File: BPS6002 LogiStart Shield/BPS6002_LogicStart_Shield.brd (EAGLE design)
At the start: 118.4 x 58.7 mm, 91 parts, among them J1 AUDIO-CONNECTOR-6P-SMD-344003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, Q1 MMBTA56, Q2 MMBTA56, Q3 MMBTA56, Q4 MMBTA56, Q5 MMBTA56

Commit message: LogicStart Shield V1.01
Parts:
- added AREF: (no value), adafruit:1X01
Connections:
- new net N$9: AREF.1, H1.AREF
- net 3V3: now also JP2.1, JP2.2, JP2.3, JP2.4, JP2.5, JP2.6
- net 5V0: no longer H1.AREF, JP2.1, JP2.2, JP2.3, JP2.4, JP2.5, JP2.6
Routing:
- net 5V0: track 135.6 -> 40.7 mm, vias 3 -> 2
- net 3V3: track 21.1 -> 31.3 mm
- net N$9: track 0.00 -> 5.21 mm
- net DIR_LEFT: track 39.7 -> 43.3 mm
- net DIR_DOWN: track 53.7 -> 56.5 mm
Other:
- board text added: "Get Started at LogicShield.GadgetFactory.Net"
- board text added: "LogicStart Shield V1.01"
- board text removed: "5V"
- board text removed: "Get Started at learn.GadgetFactory.net/LogicStart"
- board text removed: "LogicStart Shield V1.0"
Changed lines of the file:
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@@
 <layer number="220" name="220bmp" color="21" fill="1" visible="no" active="no"/>
 <layer number="221" name="221bmp" color="22" fill="1" visible="no" active="no"/>
+<layer number="222" name="222bmp" color="23" fill="1" visible="no" active="no"/>
 <layer number="223" name="223bmp" color="24" fill="1" visible="no" active="no"/>
 <layer number="224" name="224bmp" color="25" fill="1" visible="no" active="no"/>
@@
 <wire x1="1.016" y1="0" x2="1.016" y2="55.88" width="0.254" layer="20"/>
 <text x="18.288" y="41.148" size="1.778" layer="21" ratio="12">Papilio Platform</text>
-<text x="18.288" y="38.608" size="1.27" layer="21" ratio="10">LogicStart Shield V1.0</text>
+<text x="18.288" y="38.608" size="1.27" layer="21" ratio="10">LogicStart Shield V1.01</text>
 <text x="28.194" y="5.08" size="1.27" layer="21" ratio="10">www.papilio.cc BPS6002</text>
 <text x="28.194" y="7.747" size="1.27" layer="21" ratio="10">(c) GadgetFactory LLC</text>
@@
 <text x="12.0904" y="1.27" size="1.016" layer="21" font="vector" ratio="15">5</text>
 <text x="8.001" y="8.509" size="1.016" layer="21" font="vector" ratio="15">GND</text>
-<text x="8.4074" y="5.7658" size="1.016" layer="21" font="vector" ratio="15">5V</text>
+<text x="7.5184" y="5.8928" size="1.016" layer="21" font="vector" ratio="15">3.3V</text>
 <text x="16.383" y="13.462" size="1.6764" layer="21" ratio="15">DOWN</text>
 <text x="6.223" y="19.685" size="1.6764" layer="21" ratio="15">LEFT</text>
@@
 <text x="96.52" y="3.81" size="1.27" layer="25" font="vector" ratio="15">LogicStart VGA Wing</text>
 <text x="100.711" y="1.778" size="1.27" layer="21" ratio="10">www.papilio.cc</text>
-<text x="25.273" y="53.34" size="1.27" layer="21" ratio="10">Get Started at learn.GadgetFactory.net/LogicStart</text>
+<text x="25.273" y="53.34" size="1.27" layer="21" ratio="10">Get Started at LogicShield.GadgetFactory.Net</text>
 <text x="14.097" y="12.446" size="1.6764" layer="21" ratio="15" rot="R180">ANALOG</text>
 <text x="89.5096" y="43.9674" size="1.27" layer="21" font="vector" ratio="10" rot="R270">IO0</text>
@@
 </element>
 <element name="W1" library="Papilio" package="WINGSIDE_8BIT_NOHOLES" value="WING8_NOHOLES_FEMALE_TOP" x="86.36" y="6.35" rot="R180"/>
+<element name="AREF" library="adafruit" package="1X01" value="" x="23.876" y="45.593" smashed="yes">
+<attribute name="NAME" x="21.7678" y="47.2948" size="1.27" layer="25" ratio="10"/>
+<attribute name="VALUE" x="22.606" y="42.418" size="1.27" layer="27"/>
+</element>
 </elements>
 <signals>
@@
 <wire x1="76.454" y1="21.844" x2="76.2" y2="21.59" width="0.6096" layer="1"/>
 <contactref element="W1" pad="3V3@2"/>
-</signal>
-<signal name="5V0">
-<contactref element="H1" pad="5V@0"/>
 <contactref element="JP2" pad="1"/>
 <contactref element="JP2" pad="2"/>
@@
 <contactref element="JP2" pad="5"/>
 <contactref element="JP2" pad="6"/>
-<wire x1="38.1" y1="2.54" x2="38.1" y2="2.794" width="0.4064" layer="16"/>
-<wire x1="38.1" y1="2.794" x2="36.83" y2="4.064" width="0.4064" layer="16"/>
-<wire x1="36.83" y1="4.064" x2="29.21" y2="4.064" width="0.4064" layer="16"/>
-<wire x1="29.21" y1="4.064" x2="27.432" y2="2.286" width="0.4064" layer="16"/>
-<wire x1="27.432" y1="2.286" x2="17.018" y2="2.286" width="0.4064" layer="16"/>
-<wire x1="17.018" y1="2.286" x2="16.256" y2="3.048" width="0.4064" layer="16"/>
-<wire x1="16.256" y1="3.048" x2="16.256" y2="5.08" width="0.4064" layer="16"/>
-<wire x1="16.256" y1="5.08" x2="17.526" y2="6.35" width="0.4064" layer="16"/>
-<wire x1="12.446" y1="6.35" x2="12.7" y2="6.35" width="0.4064" layer="1"/>
-<wire x1="12.7" y1="6.35" x2="14.986" y2="6.35" width="0.4064" layer="1"/>
 <wire x1="25.146" y1="6.35" x2="22.606" y2="6.35" width="0.4064" layer="1"/>
 <wire x1="20.066" y1="6.35" x2="17.526" y2="6.35" width="0.4064" layer="1"/>
 <wire x1="14.986" y1="6.35" x2="17.526" y2="6.35" width="0.4064" layer="1"/>
 <wire x1="20.066" y1="6.35" x2="22.606" y2="6.35" width="0.4064" layer="16"/>
-<contactref element="H1" pad="AREF"/>
-<wire x1="23.876" y1="50.8" x2="23.876" y2="34.036" width="0.3048" layer="16"/>
-<wire x1="23.876" y1="34.036" x2="7.62" y2="17.78" width="0.3048" layer="16"/>
-<via x="7.62" y="17.78" extent="1-16" drill="0.381"/>
-<wire x1="7.62" y1="17.78" x2="7.62" y2="8.89" width="0.3048" layer="1"/>
-<wire x1="7.62" y1="8.89" x2="10.16" y2="6.35" width="0.3048" layer="1"/>
-<wire x1="12.7" y1="6.35" x2="10.16" y2="6.35" width="0.3048" layer="1"/>
+</signal>
+<signal name="5V0">
+<contactref element="H1" pad="5V@0"/>
 <contactref element="W1" pad="5V@2"/>
 <wire x1="74.93" y1="2.54" x2="73.66" y2="1.27" width="0.3048" layer="16"/>
@@
 <wire x1="19.901" y1="22.479" x2="19.774" y2="22.352" width="0.254" layer="1"/>
 <contactref element="H1" pad="D12"/>
-<wire x1="13.208" y1="34.036" x2="13.208" y2="29.718" width="0.254" layer="1"/>
+<wire x1="13.208" y1="34.798" x2="13.208" y2="29.718" width="0.254" layer="1"/>
 <wire x1="13.208" y1="29.718" x2="18.542" y2="24.384" width="0.254" layer="1"/>
 <wire x1="18.542" y1="24.384" x2="19.52" y2="24.384" width="0.254" layer="1"/>
 <wire x1="19.52" y1="24.384" x2="19.774" y2="24.13" width="0.254" layer="1"/>
-<wire x1="31.496" y1="50.8" x2="29.464" y2="48.768" width="0.254" layer="1"/>
-<wire x1="29.464" y1="48.768" x2="27.94" y2="48.768" width="0.254" layer="1"/>
-<wire x1="27.94" y1="48.768" x2="13.208" y2="34.036" width="0.254" layer="1"/>
+<wire x1="13.208" y1="34.798" x2="19.05" y2="40.64" width="0.254" layer="1"/>
+<wire x1="19.05" y1="40.64" x2="25.4" y2="40.64" width="0.254" layer="1"/>
+<wire x1="25.4" y1="40.64" x2="30.48" y2="45.72" width="0.254" layer="1"/>
+<wire x1="30.48" y1="45.72" x2="30.48" y2="49.784" width="0.254" layer="1"/>
+<wire x1="30.48" y1="49.784" x2="31.496" y2="50.8" width="0.254" layer="1"/>
 </signal>
 <signal name="DIR_RIGHT">
@@
 <wire x1="5.744" y1="27.4" x2="5.744" y2="29.785" width="0.254" layer="1"/>
 <wire x1="5.744" y1="29.785" x2="5.804" y2="29.845" width="0.254" layer="1"/>
-<wire x1="28.956" y1="50.8" x2="28.702" y2="50.8" width="0.254" layer="1"/>
-<wire x1="28.702" y1="50.8" x2="12.446" y2="34.544" width="0.254" layer="1"/>
-<wire x1="12.446" y1="34.544" x2="12.446" y2="27.498" width="0.254" layer="1"/>
+<wire x1="12.446" y1="35.306" x2="12.446" y2="27.498" width="0.254" layer="1"/>
 <wire x1="12.446" y1="27.498" x2="12.544" y2="27.4" width="0.254" layer="1"/>
+<wire x1="12.446" y1="35.306" x2="19.05" y2="41.91" width="0.254" layer="1"/>
+<wire x1="19.05" y1="41.91" x2="25.4" y2="41.91" width="0.254" layer="1"/>
+<wire x1="25.4" y1="41.91" x2="27.94" y2="44.45" width="0.254" layer="1"/>
+<wire x1="27.94" y1="44.45" x2="27.94" y2="49.784" width="0.254" layer="1"/>
+<wire x1="27.94" y1="49.784" x2="28.956" y2="50.8" width="0.254" layer="1"/>
 </signal>
 <signal name="WING_GND">
@@
 <wire x1="88.646" y1="28.702" x2="89.878" y2="28.702" width="0.254" layer="1"/>
 </signal>
+<signal name="N$9">
+<contactref element="H1" pad="AREF"/>
+<contactref element="AREF" pad="1"/>
+<wire x1="23.876" y1="50.8" x2="23.876" y2="45.593" width="0.254" layer="1"/>
+</signal>
 </signals>

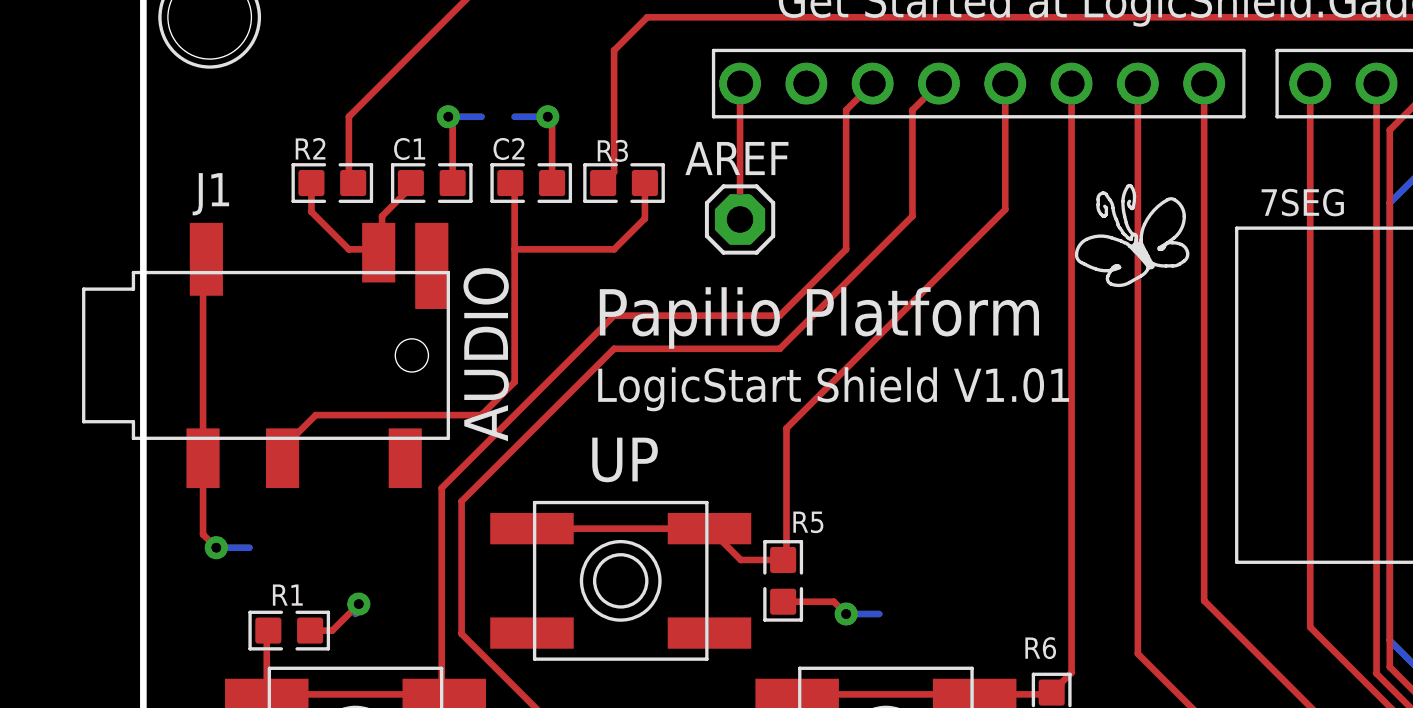
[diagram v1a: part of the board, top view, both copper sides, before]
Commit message: Fix Audio Jack.
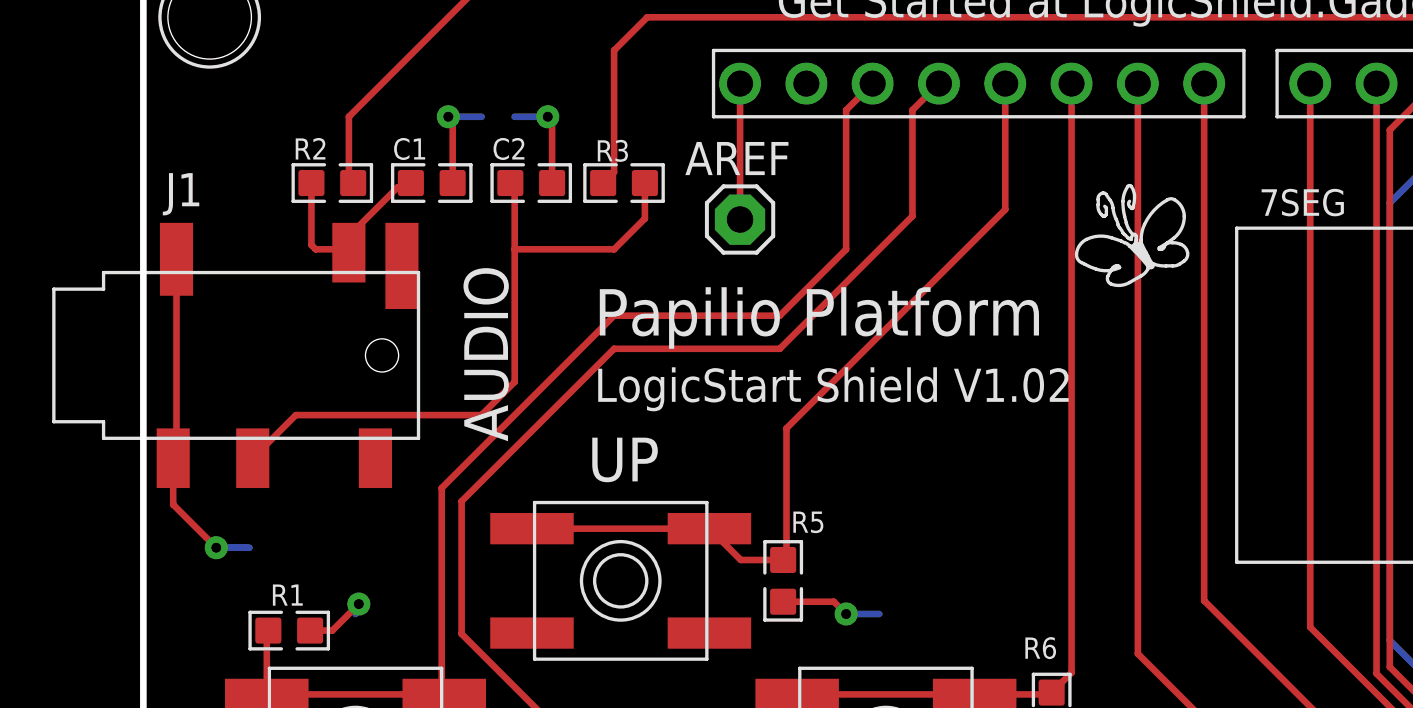
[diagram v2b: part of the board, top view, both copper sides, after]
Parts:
- moved J1 1.14 mm to (4.57, 40.4)
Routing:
- net N$33: track 24.9 -> 25.8 mm
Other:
- board text added: "LogicStart Shield V1.02"
- board text removed: "LogicStart Shield V1.01"
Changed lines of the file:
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@@
 <wire x1="1.016" y1="0" x2="1.016" y2="55.88" width="0.254" layer="20"/>
 <text x="18.288" y="41.148" size="1.778" layer="21" ratio="12">Papilio Platform</text>
-<text x="18.288" y="38.608" size="1.27" layer="21" ratio="10">LogicStart Shield V1.01</text>
+<text x="18.288" y="38.608" size="1.27" layer="21" ratio="10">LogicStart Shield V1.02</text>
 <text x="28.194" y="5.08" size="1.27" layer="21" ratio="10">www.papilio.cc BPS6002</text>
 <text x="28.194" y="7.747" size="1.27" layer="21" ratio="10">(c) GadgetFactory LLC</text>
@@
 <attribute name="PARTNO" value="RMCF0603JT10K0" x="37.846" y="18.923" size="1.778" layer="27" rot="R90" display="off"/>
 </element>
-<element name="J1" library="OPL Eagle Library" package="6P-SMD-3.5" value="AUDIO-CONNECTOR-6P-SMD-3440030P1" x="5.715" y="40.386" smashed="yes" rot="R180">
-<attribute name="PARTNO" value="3440030P1" x="5.715" y="40.386" size="1.778" layer="27" rot="R180" display="off"/>
-<attribute name="NAME" x="4.445" y="47.371" size="1.27" layer="25" ratio="12" rot="R180"/>
-<attribute name="VALUE" x="9.525" y="40.386" size="0.635" layer="27" ratio="10" rot="R180"/>
+<element name="J1" library="OPL Eagle Library" package="6P-SMD-3.5" value="AUDIO-CONNECTOR-6P-SMD-3440030P1" x="4.572" y="40.386" smashed="yes" rot="R180">
+<attribute name="PARTNO" value="3440030P1" x="4.572" y="40.386" size="1.778" layer="27" rot="R180" display="off"/>
+<attribute name="NAME" x="3.302" y="47.371" size="1.27" layer="25" ratio="12" rot="R180"/>
+<attribute name="VALUE" x="8.382" y="40.386" size="0.635" layer="27" ratio="10" rot="R180"/>
 </element>
 <element name="C1" library="GadgetFactory" package="0603" value="4700pF" x="12.065" y="46.99">
@@
 <contactref element="JP1" pad="5"/>
 <contactref element="JP1" pad="6"/>
-<wire x1="3.302" y1="36.449" x2="3.302" y2="33.528" width="0.254" layer="1"/>
-<wire x1="3.302" y1="33.528" x2="3.81" y2="33.02" width="0.254" layer="1"/>
 <via x="3.81" y="33.02" extent="1-16" drill="0.381"/>
 <wire x1="3.81" y1="33.02" x2="5.08" y2="33.02" width="0.254" layer="16"/>
-<wire x1="3.302" y1="36.449" x2="3.302" y2="43.942" width="0.254" layer="1"/>
-<wire x1="3.302" y1="43.942" x2="3.429" y2="44.069" width="0.254" layer="1"/>
 <wire x1="12.865" y1="46.99" x2="12.865" y2="49.365" width="0.254" layer="1"/>
 <wire x1="12.865" y1="49.365" x2="12.7" y2="49.53" width="0.254" layer="1"/>
@@
 <contactref element="J2" pad="5"/>
 <contactref element="W1" pad="GND@2"/>
+<wire x1="2.286" y1="44.069" x2="2.286" y2="36.576" width="0.254" layer="1"/>
+<wire x1="2.286" y1="36.576" x2="2.159" y2="36.449" width="0.254" layer="1"/>
+<wire x1="2.159" y1="36.449" x2="2.159" y2="34.671" width="0.254" layer="1"/>
+<wire x1="2.159" y1="34.671" x2="3.81" y2="33.02" width="0.254" layer="1"/>
 </signal>
 <signal name="HORIZONTAL_SYNC">
@@
 <contactref element="C1" pad="1"/>
 <contactref element="J1" pad="L"/>
-<wire x1="7.455" y1="46.99" x2="7.455" y2="45.885" width="0.254" layer="1"/>
-<wire x1="7.455" y1="45.885" x2="8.89" y2="44.45" width="0.254" layer="1"/>
-<wire x1="8.89" y1="44.45" x2="9.906" y2="44.45" width="0.254" layer="1"/>
-<wire x1="9.906" y1="44.45" x2="10.033" y2="44.323" width="0.254" layer="1"/>
 <wire x1="11.265" y1="46.99" x2="11.265" y2="46.825" width="0.254" layer="1"/>
-<wire x1="11.265" y1="46.825" x2="10.16" y2="45.72" width="0.254" layer="1"/>
-<wire x1="10.16" y1="45.72" x2="10.16" y2="44.45" width="0.254" layer="1"/>
-<wire x1="10.16" y1="44.45" x2="10.033" y2="44.323" width="0.254" layer="1"/>
+<wire x1="7.455" y1="46.99" x2="7.455" y2="44.615" width="0.254" layer="1"/>
+<wire x1="7.455" y1="44.615" x2="7.62" y2="44.45" width="0.254" layer="1"/>
+<wire x1="7.62" y1="44.45" x2="8.763" y2="44.45" width="0.254" layer="1"/>
+<wire x1="11.265" y1="46.825" x2="10.757" y2="46.825" width="0.254" layer="1"/>
+<wire x1="10.757" y1="46.825" x2="8.763" y2="44.831" width="0.254" layer="1"/>
+<wire x1="8.763" y1="44.831" x2="8.763" y2="44.45" width="0.254" layer="1"/>
+<wire x1="8.763" y1="44.45" x2="8.89" y2="44.323" width="0.254" layer="1"/>
 </signal>
 <signal name="AUDIO-LEFT">
@@
 <contactref element="C2" pad="1"/>
 <contactref element="J1" pad="R"/>
-<wire x1="6.35" y1="36.449" x2="6.35" y2="36.83" width="0.254" layer="1"/>
-<wire x1="6.35" y1="36.83" x2="7.62" y2="38.1" width="0.254" layer="1"/>
-<wire x1="7.62" y1="38.1" x2="13.97" y2="38.1" width="0.254" layer="1"/>
+<wire x1="6.858" y1="38.1" x2="13.97" y2="38.1" width="0.254" layer="1"/>
 <wire x1="13.97" y1="38.1" x2="15.24" y2="39.37" width="0.254" layer="1"/>
 <wire x1="15.24" y1="39.37" x2="15.24" y2="44.45" width="0.254" layer="1"/>
@@
 <wire x1="20.231" y1="45.631" x2="19.05" y2="44.45" width="0.254" layer="1"/>
 <wire x1="19.05" y1="44.45" x2="15.24" y2="44.45" width="0.254" layer="1"/>
+<wire x1="6.858" y1="38.1" x2="5.207" y2="36.449" width="0.254" layer="1"/>
 </signal>
 <signal name="AUDIO-RIGHT">
